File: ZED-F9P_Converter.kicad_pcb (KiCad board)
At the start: 2 copper layers, 41.5 x 34 mm, 5 parts, among them J1 Conn_01x14, J2 Conn_01x13, J3 Conn_01x14, J4 Conn_01x13, U1 Ublox_ZED_F9P

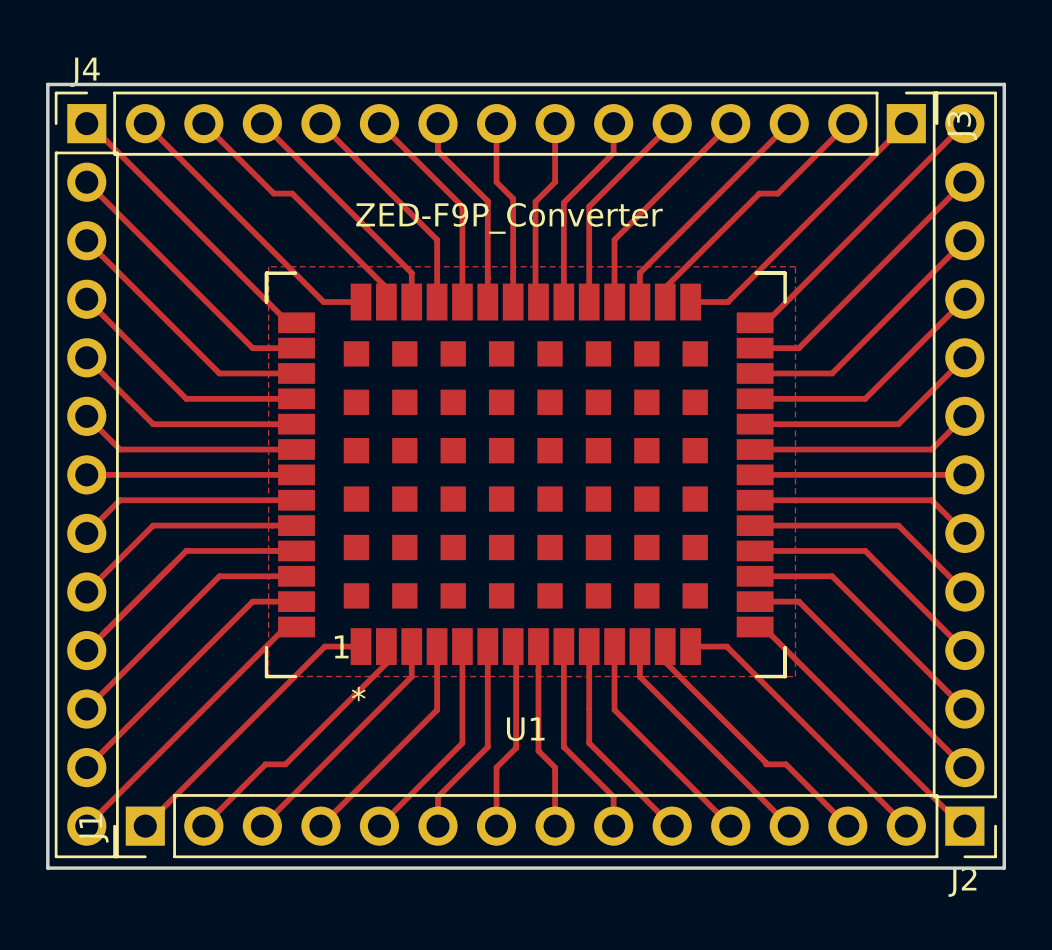
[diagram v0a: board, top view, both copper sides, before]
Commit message: 線幅0.5mmに変更
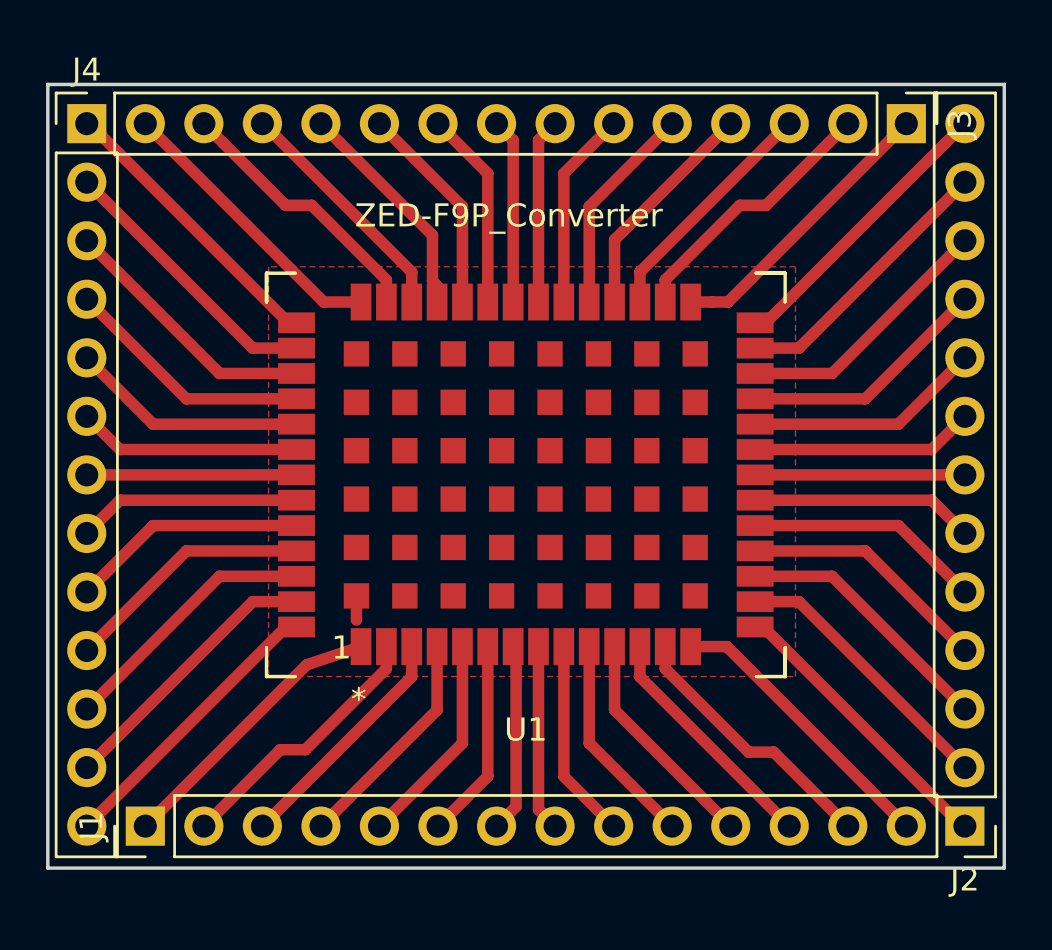
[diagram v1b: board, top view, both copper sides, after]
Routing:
- net GND: track 86.3 -> 87.3 mm
